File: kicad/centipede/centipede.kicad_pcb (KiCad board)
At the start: 2 copper layers, 300 x 300 mm, 13 parts

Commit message: Deepen the Centipede and Battlezone board maps
Centipede gains sheet 02A: the playfield address selector and the eight
2101A-2 playfield RAMs, taking it from 13 devices to 23. The sheet also carries
a complete playfield RAM test — CAT Box switch settings, key in 0400, and a lit
COMPARE ERROR LED gives the failing address directly.

Battlezone gains sheet 02B: both 8-position option switch banks (M10 read by
N11 via OPT0, P10 read by P11 via OPT1), the coin door input buffer and the
Y-axis DAC. 23 devices to 31.

Worth knowing from that sheet: R11 buffers the coin door inputs *and* 3KHZ and
HALT, so a machine that will not coin up and one reporting a bad
vector-generator state can share a single failed buffer.

Adds tools/publish_board.py — interactive view, BOM and site registration in
one command, rather than three ad-hoc snippets per board.

Co-Authored-By: Claude Opus 5 <noreply@anthropic.com>
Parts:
- added UK5: 2101A-2, DIP-14_W7.62mm, F.Cu at (127.6, 132.3)
- added UK7: 2101A-2, DIP-14_W7.62mm, F.Cu at (178.4, 132.3)
- added UL5: 2101A-2, DIP-14_W7.62mm, F.Cu at (127.6, 113.2)
- added UL7: 2101A-2, DIP-14_W7.62mm, F.Cu at (178.4, 113.2)
- added UM5: 2101A-2, DIP-14_W7.62mm, F.Cu at (127.6, 94.2)
- added UM7: 2101A-2, DIP-14_W7.62mm, F.Cu at (178.4, 94.2)
- added UN5: 2101A-2, DIP-14_W7.62mm, F.Cu at (127.6, 75.2)
- added UN7: 2101A-2, DIP-14_W7.62mm, F.Cu at (178.4, 75.2)
- added UP5: 74LS157, DIP-14_W7.62mm, F.Cu at (127.6, 56.1)
- added UP7: 74LS257, DIP-14_W7.62mm, F.Cu at (178.4, 56.1)

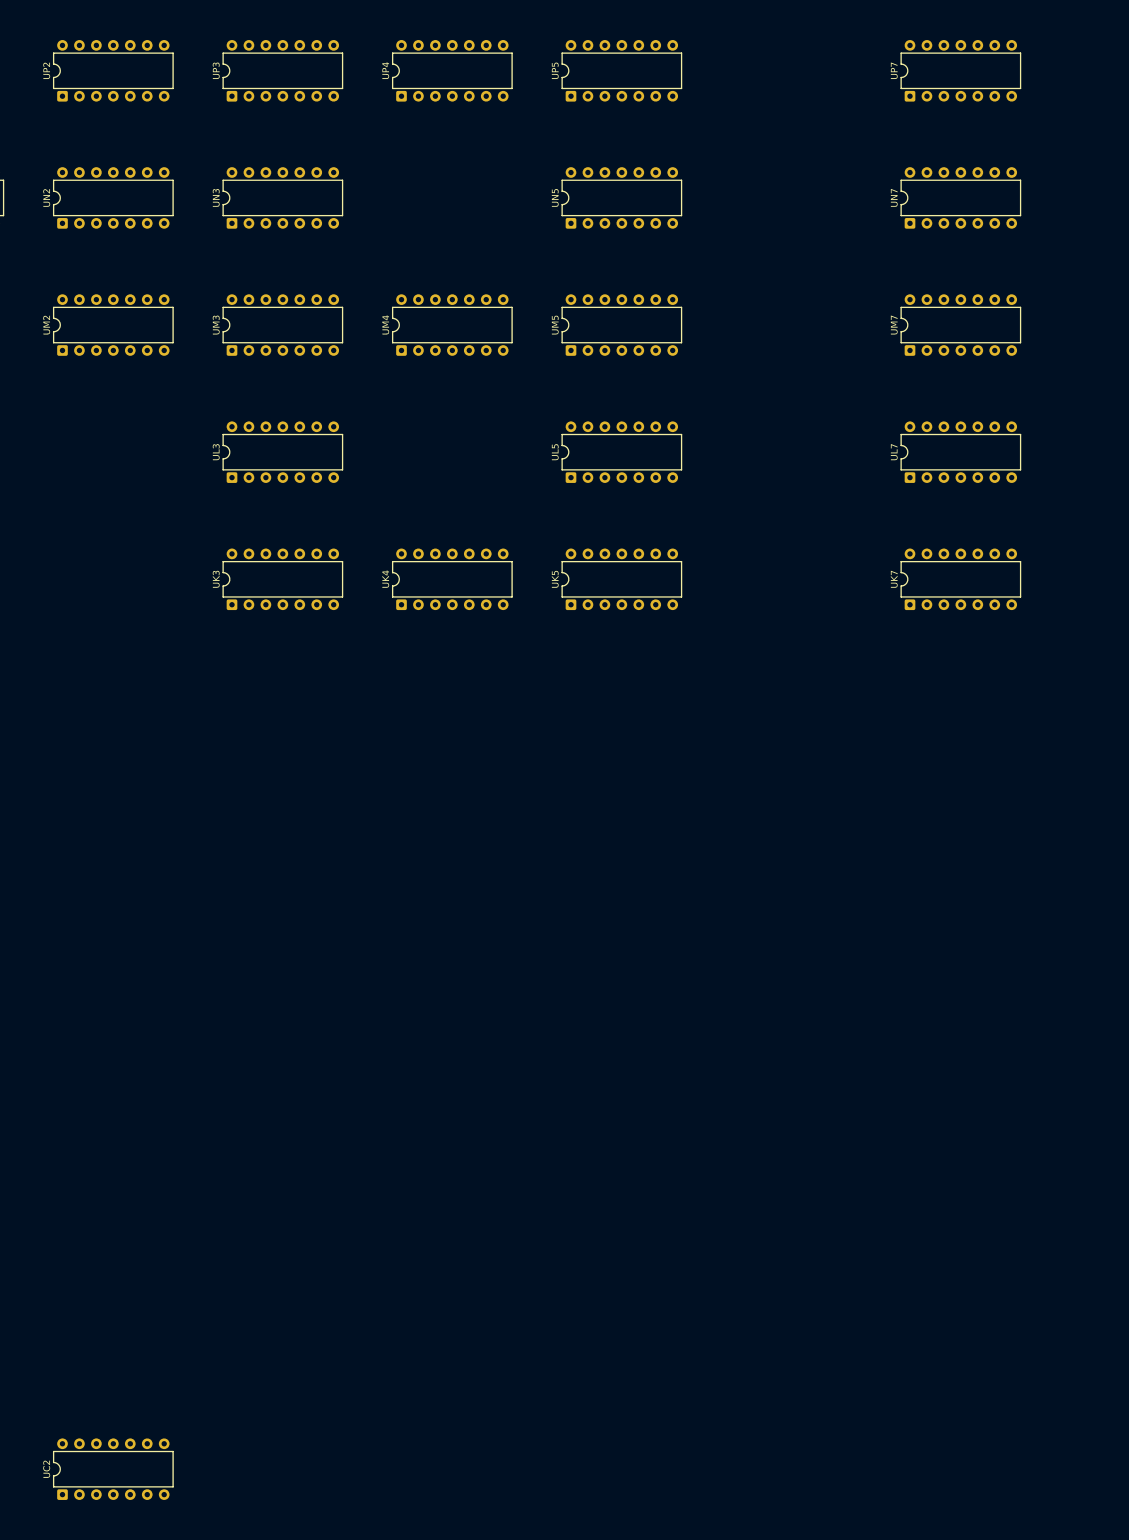
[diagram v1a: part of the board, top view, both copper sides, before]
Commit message: Draw every device at its real package size
The board maps existed to answer "which chip is at C4", and then drew a
24-pin ROM and a 20-pin LS245 as the same 14-pin outline. package_for()
read pin counts from DEVICES, which holds 20 Pong-era parts against the
112 part types the boards actually use, and silently fell back to DIP-14
for the other 92.

tools/packages.py is the pin-count table, kept separate from devices.py
on purpose: packaging needs one number for every part on every board,
while devices.py carries verified pinouts for the parts validate_nets.py
reasons about, and widening that set to satisfy a drawing would let the
extractor trust readings nothing has checked.

688 of 704 devices now size. check_packages.py re-derives 56 of the
entries from KiCAD's symbol library — comparing the highest pin number,
not the pin count, since KiCAD omits no-connects and a 7493 symbol has
ten pins on a DIP-14 — and confirms all 20 parts in DEVICES agree. The
Am2901 slices and the POKEY come from DIP-40 stated on the Battlezone
sheet; the 8316E from the drawing's note that a 2708 may be fitted
instead.

What does not size is now said out loud rather than quietly drawn at 14
pins: four descriptions recorded where the sheet gave no part number,
and the Atari 0351xx ROM/PROM numbers, which get the class default and
are listed as unverified until someone has a board in front of them.

Two things found while reading the corpus for packages, both logged in
asteroids.read.json rather than acted on. The -06 rate multiplier
resolution was recorded and never applied to the board data, and the
parts list disagrees with both readings on designators. F4/H4/J4 take
either an LS670 or an LS170, and the 19-007 pull-up network is fitted
only with the LS170 — same package either way, but a real failure mode.

Also: republishing a board without --machine used to unlink it from its
machine, because most definitions carry no machine of their own and the
link lived only in boards.json. publish_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
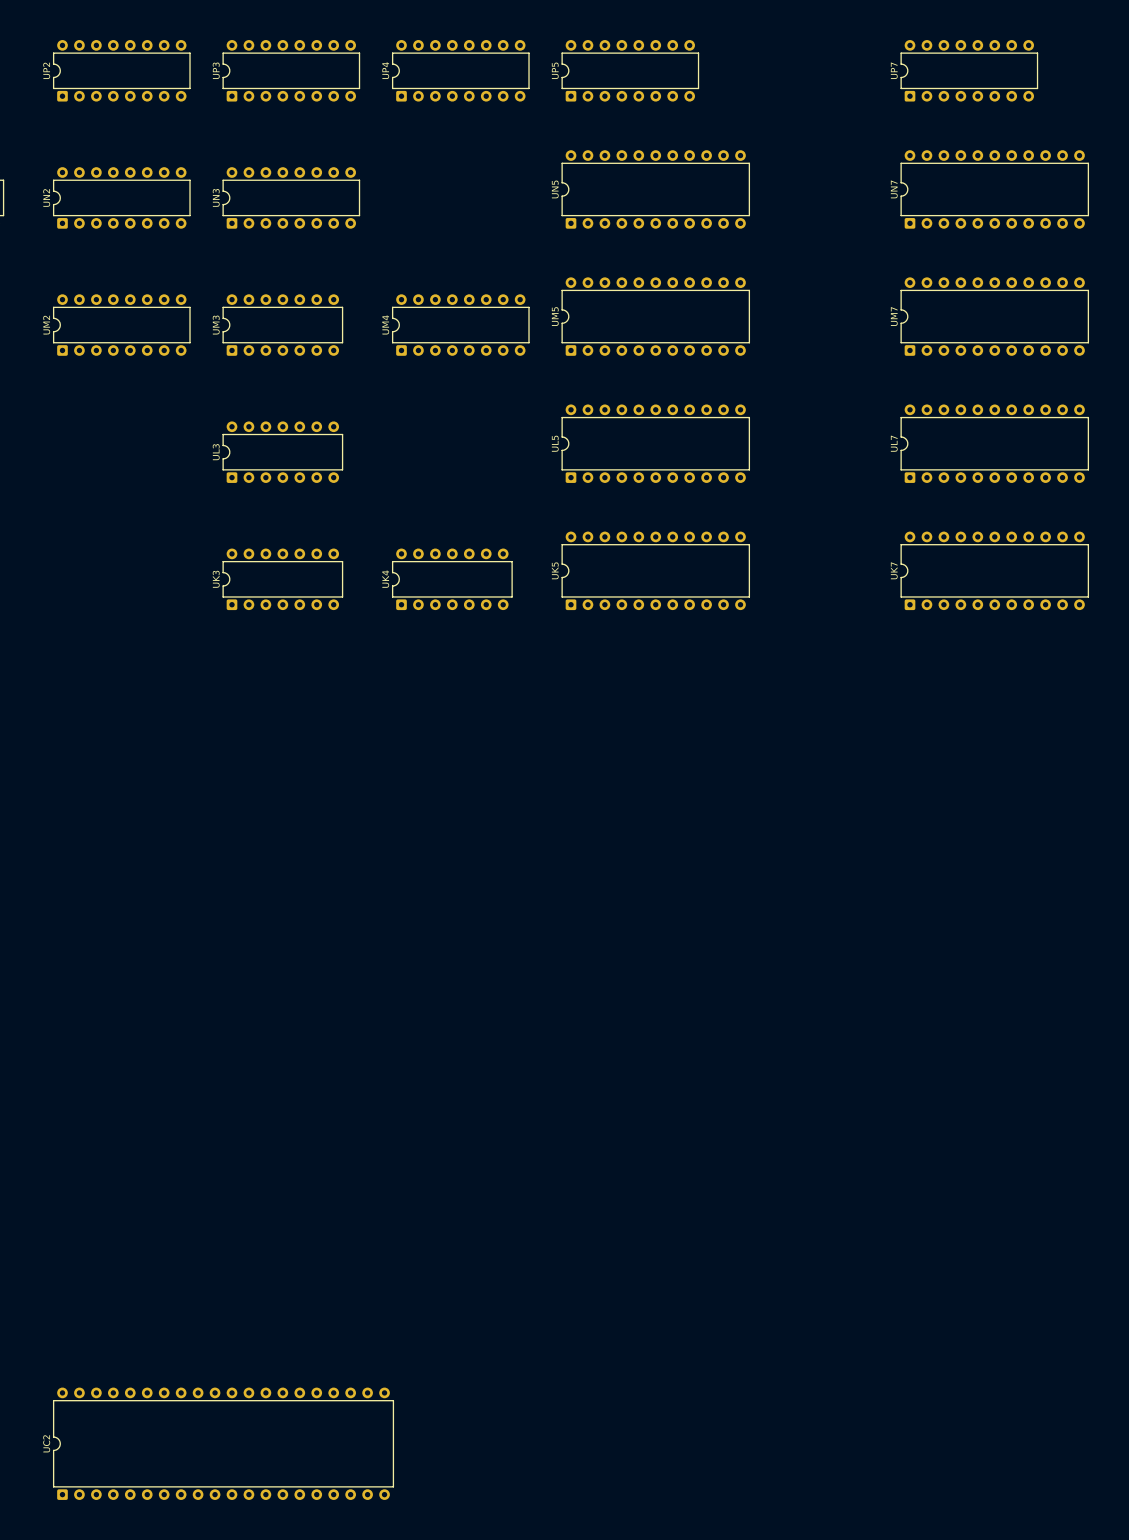
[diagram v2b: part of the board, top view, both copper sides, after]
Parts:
- UC2: footprint DIP-14_W7.62mm -> DIP-40_W15.24mm
- UK5, UK7, UL5, UL7, UM5, UM7, UN5, UN7: footprint DIP-14_W7.62mm -> DIP-22_W10.16mm
- UM2, UM4, UN2, UN3, UP2, UP3, UP4, UP5, UP7: footprint DIP-14_W7.62mm -> DIP-16_W7.62mm

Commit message: Drop two grid rows that do not exist, and span the devices that do
Atari's grid alphabet skips G, I, O and Q, and the board definitions
listed G and Q as rows. Every device below F was therefore drawn a row
too low, the rendered board carried two empty bands, and F/H1 looked
like a three-position span for a part 1.2in long on a 0.75in pitch.

Confirmed three ways before touching it. Nothing in any read, signature
or signal record in this repo sits in a G or Q row, while both
neighbours of each are populated on the two densest boards — Battlezone
P:6 R:2, Asteroids-03 P:4 R:3. The sheets' own spanning designators
treat F and H as adjacent and H and J as adjacent, which is only
possible if G and I are not positions. And with G removed, F/H falls out
as an adjacent pair, which is what a 24-pin ROM needs. Pong predates the
convention and legitimately uses G, so it keeps its grid.

Spans are now data rather than prose. A device drawn across two or three
cells is still keyed at its first cell, because that is the only thing
`ics` may be keyed by, but the sheet's own designator goes in a `spans`
map and the footprint is placed at the mean of the cells it names. A
DIP-40 at B/C2 sits between B2 and C2 instead of hanging equally over A2
and C2. The build rejects a span whose rows are not adjacent — that
failure almost always means the grid is wrong, not the span.

Two more inconsistencies found and logged rather than guessed at. Two of
the Math Box's four Am2901 slices carry a span and two do not, though
all four are the same DIP-40 on the same pitch. And asteroids-04.json
carries five devices at the -03 PROM positions alongside the -04 ROMs
and is missing 035144-02 at D/E1, contradicting the substitution table,
memory_by_revision and its own status text in the same breath.

Co-Authored-By: Claude Opus 5 <noreply@anthropic.com>
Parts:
- moved UC2 38.1 mm to (51.4, 227.6)
- moved UK3 19.1 mm to (76.8, 113.2)
- moved UK4 19.1 mm to (102.2, 113.2)
- moved UK5 19.1 mm to (127.6, 113.2)
- moved UK7 19.1 mm to (178.4, 113.2)
- moved UN1 19.1 mm to (26.0, 56.1)
- moved UN2 19.1 mm to (51.4, 56.1)
- moved UN3 19.1 mm to (76.8, 56.1)
- moved UN5 19.1 mm to (127.6, 56.1)
- moved UN7 19.1 mm to (178.4, 56.1)
- moved UP2 19.1 mm to (51.4, 37.0)
- moved UP3 19.1 mm to (76.8, 37.0)
- moved UP4 19.1 mm to (102.2, 37.0)
- moved UP5 19.1 mm to (127.6, 37.0)
- moved UP7 19.1 mm to (178.4, 37.0)
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
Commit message: Unlock Centipede and Tempest on a hyphen
Checking whether mikesarcade.com had anything this corpus lacks turned
up something better: Centipede and Tempest harvested nothing at all,
from forty-six and thirty-seven documents each, while Asteroids and
Battlezone gave up eighty to a hundred designators apiece. Same
manufacturer, same era, same parts-list format.

The difference was one character. Asteroids writes 'Type 74LS04
Integrated Circuit (B5)'; Centipede and Tempest write 'Type-74LS04'. The
type pattern required whitespace, so those rows never matched, fell
through to the count layout, found no leading quantity, and were
discarded silently.

Centipede goes from 23 devices to 87, Tempest from 18 to 83. Both
agree with themselves across every printing with no split, and both
confirm every drawing device the lists also name. Tempest needs
--figure: its manual carries an Auxiliary PCB alongside the
vector-generator board, and only the latter has a map.

Two more readings resolved against the drawing, on the same evidence as
Missile Command's D3. Centipede M4 is a 74LS175, not a 74LS75 — nine
printings, and 75 against 175 is a dropped digit. Tempest L6 is a
74LS670, not a 74LS14: four printings put it in a bank of three register
files at K6, L6 and M6, which is the same trio Asteroids has at F4, H4
and J4 on the same vector generator, so the grouping is coherent as well
as attested.

74LS373 and the CD4584B join the packaging table. 1,461 devices across
27 boards, all sized, none contradicted by a socket entry.

Co-Authored-By: Claude Opus 5 <noreply@anthropic.com>
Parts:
- added UA10: 7407, DIP-14_W7.62mm, F.Cu at (254.6, 256.1)
- added UA4: 74LS32, DIP-14_W7.62mm, F.Cu at (102.2, 265.6)
- added UA5: 74LS163A, DIP-16_W7.62mm, F.Cu at (127.6, 265.6)
- added UA7: 74LS20, DIP-14_W7.62mm, F.Cu at (178.4, 265.6)
- added UA8: 74LS175, DIP-16_W7.62mm, F.Cu at (203.8, 265.6)
- added UA9: 7407, DIP-14_W7.62mm, F.Cu at (229.2, 265.6)
- added UB1: 74LS244, DIP-20_W7.62mm, F.Cu at (26.0, 246.6)
- added UB11: 74LS191, DIP-16_W7.62mm, F.Cu at (280.0, 246.6)
- added UB4: 74LS273, DIP-20_W7.62mm, F.Cu at (102.2, 246.6)
- added UB5: 74LS163A, DIP-16_W7.62mm, F.Cu at (127.6, 246.6)
- added UB7: 74LS08, DIP-14_W7.62mm, F.Cu at (178.4, 246.6)
- added UC1: 74LS244, DIP-20_W7.62mm, F.Cu at (26.0, 227.6)
- added UC11: 74LS191, DIP-16_W7.62mm, F.Cu at (280.0, 227.6)
- added UC4: 74LS139, DIP-16_W7.62mm, F.Cu at (102.2, 227.6)
- added UC5: 74LS32, DIP-14_W7.62mm, F.Cu at (127.6, 227.6)
- added UC6: 74LS174, DIP-16_W7.62mm, F.Cu at (153.0, 227.6)
- added UC7: 74LS153, DIP-16_W7.62mm, F.Cu at (178.4, 227.6)
- added UD10: 74LS257, DIP-16_W7.62mm, F.Cu at (254.6, 199.0)
- added UD4: 74LS74, DIP-14_W7.62mm, F.Cu at (102.2, 208.5)
- added UD6: 74LS174, DIP-16_W7.62mm, F.Cu at (153.0, 208.5)
- added UD7: 74LS157, DIP-16_W7.62mm, F.Cu at (178.4, 208.5)
- added UD8: 74LS157, DIP-16_W7.62mm, F.Cu at (203.8, 208.5)
- added UD9: 74LS257, DIP-16_W7.62mm, F.Cu at (229.2, 208.5)
- added UE2: 74LS245, DIP-20_W7.62mm, F.Cu at (51.4, 189.4)
- added UE3: 74LS32, DIP-14_W7.62mm, F.Cu at (76.8, 189.4)
- added UE4: 74LS175, DIP-16_W7.62mm, F.Cu at (102.2, 189.4)
- added UE6: 74LS174, DIP-16_W7.62mm, F.Cu at (153.0, 189.4)
- added UE7: 74LS86, DIP-14_W7.62mm, F.Cu at (178.4, 189.4)
- added UE8: 74LS153, DIP-16_W7.62mm, F.Cu at (203.8, 189.4)
- added UE9: 74S74, DIP-14_W7.62mm, F.Cu at (229.2, 189.4)
- added UF10: 4584B, DIP-14_W7.62mm, F.Cu at (254.6, 170.4)
- added UF11: 4584B, DIP-14_W7.62mm, F.Cu at (280.0, 170.4)
- added UF3: 74LS32, DIP-14_W7.62mm, F.Cu at (76.8, 170.4)
- added UF6: 74LS83, DIP-16_W7.62mm, F.Cu at (153.0, 170.4)
- added UF8: 74LS157, DIP-16_W7.62mm, F.Cu at (203.8, 170.4)
- added UF9: 74S74, DIP-14_W7.62mm, F.Cu at (229.2, 170.4)
- added UH3: 74LS42, DIP-16_W7.62mm, F.Cu at (76.8, 151.3)
- added UH4: 74LS374, DIP-20_W7.62mm, F.Cu at (102.2, 151.3)
- added UH5: 74LS244, DIP-20_W7.62mm, F.Cu at (127.6, 151.3)
- added UH6: 74LS83, DIP-16_W7.62mm, F.Cu at (153.0, 151.3)
- added UH8: 74LS157, DIP-16_W7.62mm, F.Cu at (203.8, 151.3)
- added UH9: 74LS166, DIP-16_W7.62mm, F.Cu at (229.2, 151.3)
- added UJ2: 74LS139, DIP-16_W7.62mm, F.Cu at (51.4, 132.3)
- added UJ3: 74LS32, DIP-14_W7.62mm, F.Cu at (76.8, 132.3)
- added UJ4: 74LS174, DIP-16_W7.62mm, F.Cu at (102.2, 132.3)
- added UJ5: 74LS373, DIP-20_W7.62mm, F.Cu at (127.6, 132.3)
- added UJ6: 74LS273, DIP-20_W7.62mm, F.Cu at (153.0, 132.3)
- added UJ8: 74LS157, DIP-16_W7.62mm, F.Cu at (203.8, 132.3)
- added UJ9: 74LS166, DIP-16_W7.62mm, F.Cu at (229.2, 132.3)
- added UK2: 74LS10, DIP-14_W7.62mm, F.Cu at (51.4, 113.2)
- added UK6: 74LS153, DIP-16_W7.62mm, F.Cu at (153.0, 113.2)
- added UK8: 74LS157, DIP-16_W7.62mm, F.Cu at (203.8, 113.2)
- added UK9: 74LS257, DIP-16_W7.62mm, F.Cu at (229.2, 113.2)
- added UL2: 74LS90, DIP-14_W7.62mm, F.Cu at (51.4, 94.2)
- added UL6: 74LS153, DIP-16_W7.62mm, F.Cu at (153.0, 94.2)
- added UL8: 74LS00, DIP-14_W7.62mm, F.Cu at (203.8, 94.2)
- added UL9: 74LS257, DIP-16_W7.62mm, F.Cu at (229.2, 94.2)
- added UM10: 74LS259, DIP-16_W7.62mm, F.Cu at (254.6, 75.2)
- added UM6: 74LS153, DIP-16_W7.62mm, F.Cu at (153.0, 75.2)
- added UM8: 74LS257, DIP-16_W7.62mm, F.Cu at (203.8, 75.2)
- added UM9: 74LS257, DIP-16_W7.62mm, F.Cu at (229.2, 75.2)
- added UN4: 74LS175, DIP-16_W7.62mm, F.Cu at (102.2, 56.1)
- added UN6: 74LS153, DIP-16_W7.62mm, F.Cu at (153.0, 56.1)
- added UP6: 74LS153, DIP-16_W7.62mm, F.Cu at (153.0, 37.0)
- UM4: value 74LS75 -> 74LS175

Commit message: Take Centipede's ROMs from MAME, where two sources agree
MAME helps for exactly one thing, and it is a thing this corpus is bad
at: ROM and PROM positions. Its romset filenames carry the board
position as a suffix — '136001-409.fh1' — and they come from real
dumped boards. It knows nothing about the 74-series parts that are 95%
of a board, because it does not model them.

Centipede's map had nothing at any of its six ROM positions: the parts
lists give IC stock numbers and ROMs are not stocked that way, so the
harvest could never have found them. MAME names D1, E1, F/H1, J1, F7 and
H/J7, and the manual's own 24-contact socket entries name the same six
independently. Two sources that share no ancestry, agreeing on position
and package, so they are placed. Centipede goes 87 to 93.

Two things logged rather than acted on. Centipede's P4 is recorded as an
82S123, but MAME's dump there is 256 bytes and an 82S123 holds 32 — the
package is right either way, both being DIP-16 and the socket entry
16-contact, but the part number probably is not. And C3 and E5 have
sockets, 40-contact and 22-contact, with nothing in the map; a 40-pin
part beside the 6502 at C2 is very likely the POKEY, but nothing read so
far names it.

On Battlezone MAME confirms every ROM and PROM position exactly,
including the 82S129 at K7 and the 82S123 at B1 that were read off the
sheets by hand. It also shows only two of the four vector-ROM positions
populated — A3 and B/C3, with E3 and F/H3 empty on Battlezone and on
both Red Baron sets. That is now on the board, because chasing a chip
that was never fitted is a bad afternoon.

Co-Authored-By: Claude Opus 5 <noreply@anthropic.com>
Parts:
- added UD1: 136001-407, DIP-24_W15.24mm, F.Cu at (26.0, 208.5)
- added UE1: 136001-408, DIP-24_W15.24mm, F.Cu at (26.0, 189.4)
- added UF1: 136001-409, DIP-24_W15.24mm, F.Cu at (26.0, 160.9)
- added UF7: 136001-211, DIP-24_W15.24mm, F.Cu at (178.4, 170.4)
- added UH7: 136001-212, DIP-24_W15.24mm, F.Cu at (178.4, 141.8)
- added UJ1: 136001-410, DIP-24_W15.24mm, F.Cu at (26.0, 132.3)
